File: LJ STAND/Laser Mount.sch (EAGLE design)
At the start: 1 part

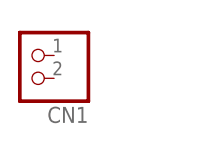
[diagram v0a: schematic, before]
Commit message: Gyro MPU9250 boards
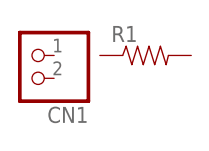
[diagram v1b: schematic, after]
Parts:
- added R1: (no value), SparkFun-Resistors:RESISTOR0603
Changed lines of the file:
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@@
 <parts>
 <part name="CN1" library="adafruit" deviceset="JST_2PIN" device="-THM-RA"/>
+<part name="R1" library="SparkFun-Resistors" deviceset="RESISTOR" device="0603"/>
 </parts>
 <sheets>
@@
 <instances>
 <instance part="CN1" gate="G$1" x="48.26" y="60.96" rot="R180"/>
+<instance part="R1" gate="G$1" x="60.96" y="60.96"/>
 </instances>
 <busses>
